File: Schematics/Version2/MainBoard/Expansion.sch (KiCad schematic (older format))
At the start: 6 parts, among them J16 Device 2, J17 Device 5, J18 Device 3, J19 Device 6, J20 Device 4, J21 Device 7

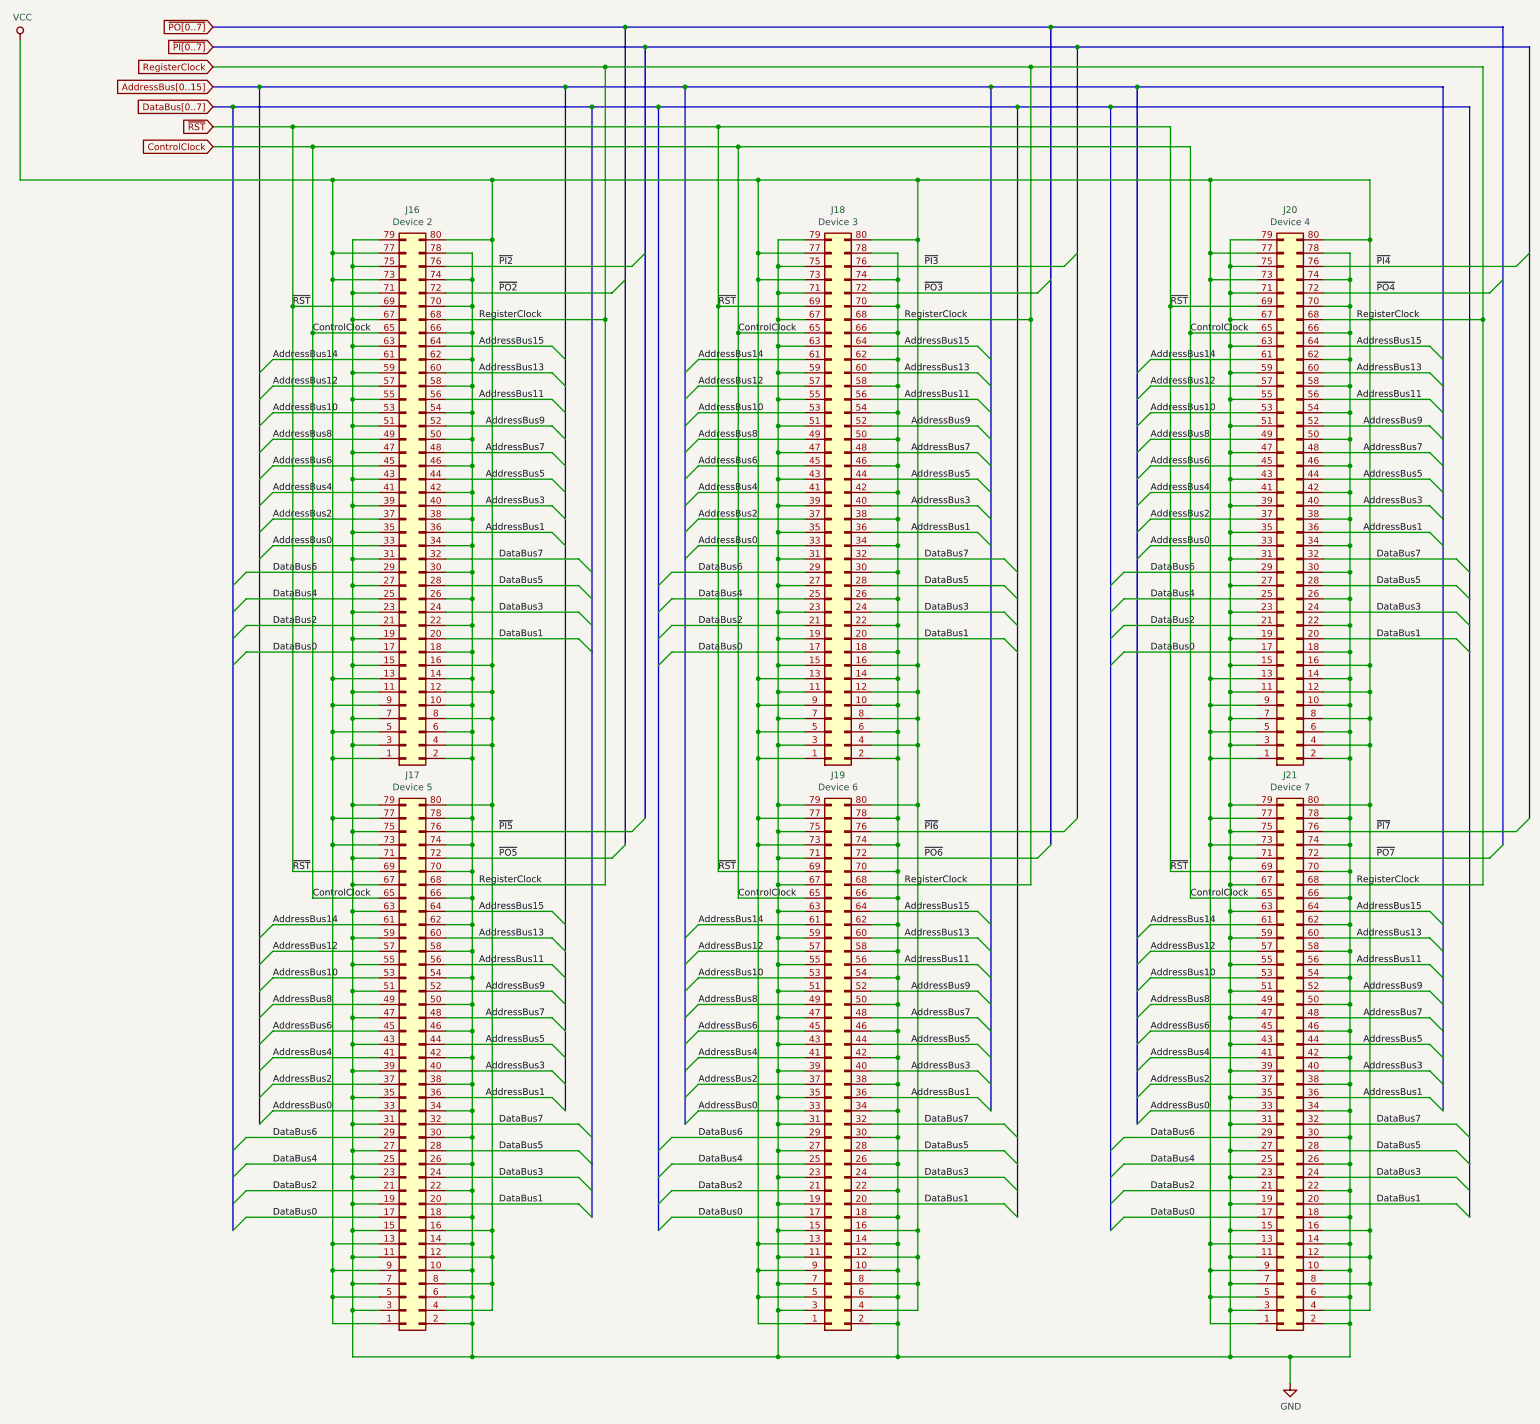
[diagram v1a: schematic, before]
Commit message: Merge branch "version2b".
This is a new version of the computer which incorporates a number of
improvements:
  * Uses a four layer PCB instead of six.
  * Replaced the clock with a new circuit. This is simpler, but allows for
    an external clock to be attached.
  * Changes to the ALU to have it operate over two clock cycles instead of
    one. This fixes a timing issue which makes the ALU unreliable at 10MHz.
  * Replaced instruction RAM with dual port SRAM.
  * Replaced the physical connector for expansion cards to interleave
    signals with ground.
  * Added places where components can be attached to provide AC termination
    of the data bus, should this be necessary.
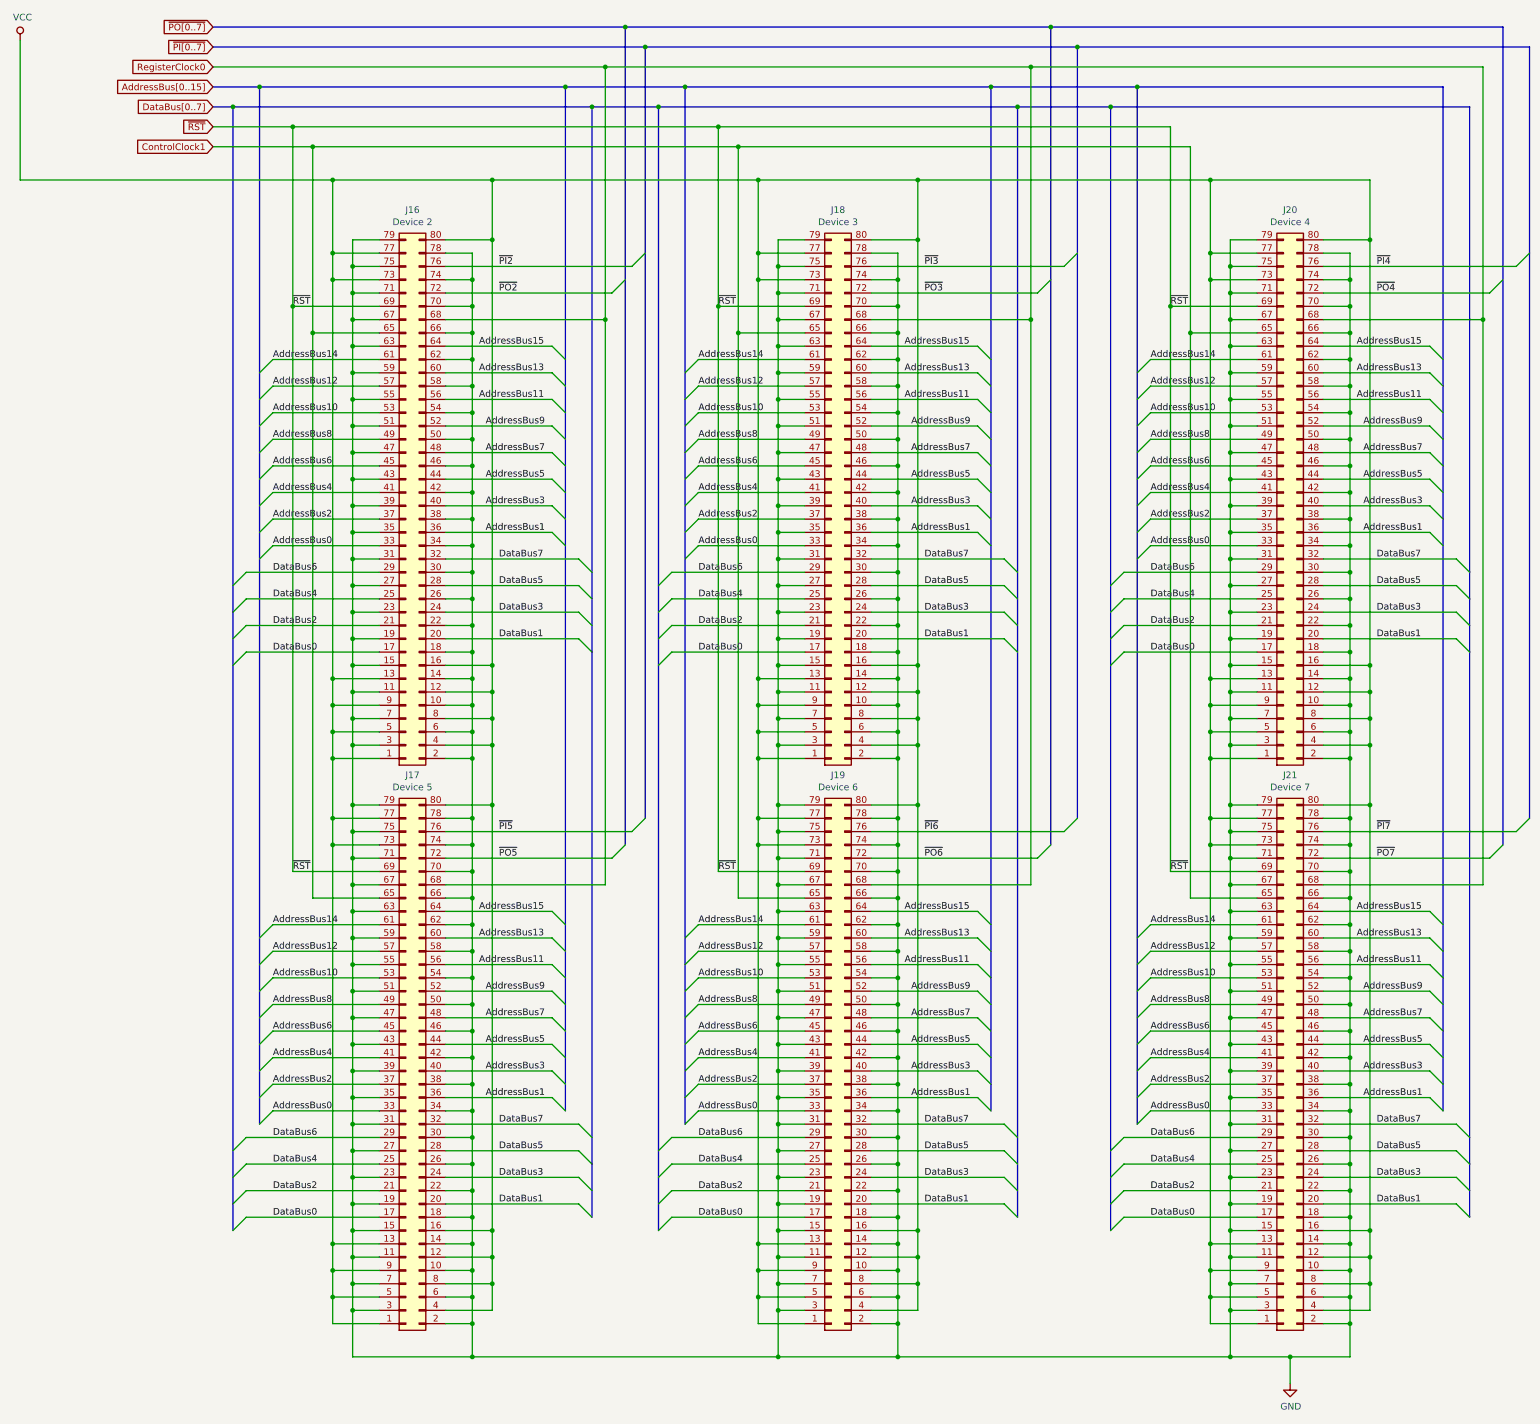
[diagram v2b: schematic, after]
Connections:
- net ControlClock renamed ControlClock1
- net RegisterClock renamed RegisterClock0
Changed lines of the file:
@@
 $Descr A3 16535 11693
 encoding utf-8
-Sheet 17 23
+Sheet 14 21
 Title "Expansion"
 Date ""
@@
 $EndDescr
 Text GLabel 2550 950  0    50   Input ~ 0
-RegisterClock
+RegisterClock0
 Text GLabel 2550 650  0    50   Input ~ 0
 ~PO[0..7]
@@
 Text Label 4700 2650 0    50   ~ 0
 ~PO2
-Text Label 4550 2850 0    50   ~ 0
-RegisterClock
 Text GLabel 2550 1250 0    50   Input ~ 0
 DataBus[0..7]
@@
 Text Label 4700 6900 0    50   ~ 0
 ~PO5
-Text Label 4550 7100 0    50   ~ 0
-RegisterClock
 Entry Wire Line
 	5300 9500 5400 9600
@@
 Text Label 7900 2650 0    50   ~ 0
 ~PO3
-Text Label 7750 2850 0    50   ~ 0
-RegisterClock
 Entry Wire Line
 	8500 5250 8600 5350
@@
 Text Label 7900 6900 0    50   ~ 0
 ~PO6
-Text Label 7750 7100 0    50   ~ 0
-RegisterClock
 Entry Wire Line
 	8500 9500 8600 9600
@@
 Entry Wire Line
 	11900 9500 12000 9600
-Text Label 11150 7100 0    50   ~ 0
-RegisterClock
 Text Label 11300 6900 0    50   ~ 0
 ~PO7
@@
 Entry Wire Line
 	11900 5250 12000 5350
-Text Label 11150 2850 0    50   ~ 0
-RegisterClock
 Text Label 11300 2450 0    50   ~ 0
 ~PI4
@@
 ~RST
 Text GLabel 2550 1550 0    50   Input ~ 0
-ControlClock
+ControlClock1
 Wire Wire Line
 	3800 2950 3300 2950
@@
 	9750 7000 10400 7000
 Connection ~ 9750 2750
-Text Label 9900 7200 0    50   ~ 0
-ControlClock
-Text Label 9900 2950 0    50   ~ 0
-ControlClock
-Text Label 6500 2950 0    50   ~ 0
-ControlClock
-Text Label 6500 7200 0    50   ~ 0
-ControlClock
-Text Label 3300 7200 0    50   ~ 0
-ControlClock
-Text Label 3300 2950 0    50   ~ 0
-ControlClock
 Text Label 3150 2750 0    50   ~ 0
 ~RST
